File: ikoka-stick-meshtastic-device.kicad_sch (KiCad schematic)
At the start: 26 parts, among them J1 Conn_Coaxial, J2 Conn_01x07_Socket, J3 Conn_01x07_Socket, J4 Conn_01x02, J5 Conn_01x02, J6 Conn_01x04, Q1 AO3401A, SW1 SW_Push, U1 MT3608, U2 E22-900M30S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

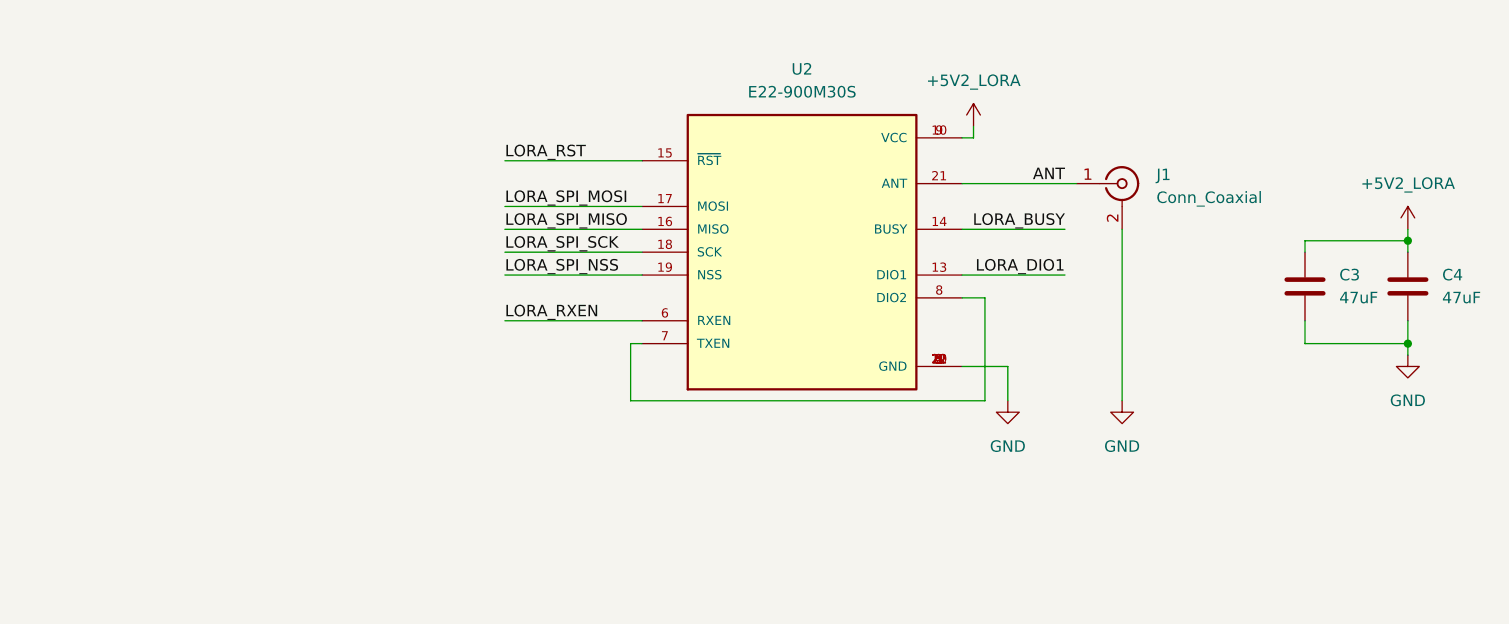
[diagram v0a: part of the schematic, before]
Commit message: Modification to support E22P modules
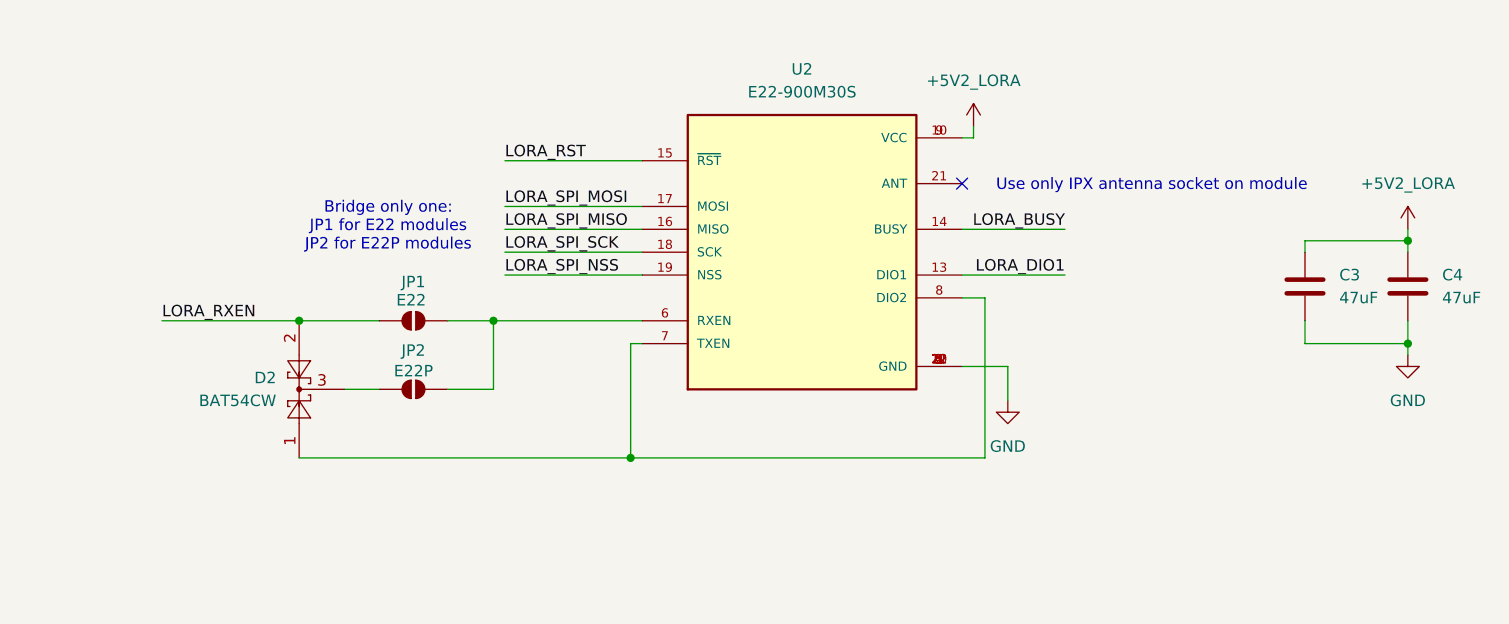
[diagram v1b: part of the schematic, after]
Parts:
- removed J1: Conn_Coaxial, Connector_Coaxial:SMA_Samtec_SMA-J-P-H-ST-EM1_EdgeMount, symbol Connector:Conn_Coaxial
- added D2: BAT54CW, Package_TO_SOT_SMD:SOT-323_SC-70, symbol Diode:BAT54CW
- added JP1: E22, Jumper:SolderJumper-2_P1.3mm_Open_RoundedPad1.0x1.5mm, symbol Jumper:SolderJumper_2_Open
- added JP2: E22P, Jumper:SolderJumper-2_P1.3mm_Open_RoundedPad1.0x1.5mm, symbol Jumper:SolderJumper_2_Open
- BT1: now left out of the parts list
- U2: footprint E22-900M30S:XCVR_E22-900M30S -> E22-900M30S:XCVR_E22-900M30S_NO_ANT; now left out of the parts list
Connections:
- net LORA_RXEN: now also D2.2, JP1.1 (A); no longer U2.6 (RXEN)
- net at U2.7 (TXEN), U2.8 (DIO2): now also D2.1
- net ANT: no longer names the net of U2.21 (ANT)
- new net: D2.3, JP2.1 (A)
- new net: JP1.2 (B), JP2.2 (B), U2.6 (RXEN)
- no-connect marks 2 -> 3
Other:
- note added: "Bridge only one: JP1 for E22 modules JP2 for E22P modules"
- note added: "Use only IPX antenna socket on module"
